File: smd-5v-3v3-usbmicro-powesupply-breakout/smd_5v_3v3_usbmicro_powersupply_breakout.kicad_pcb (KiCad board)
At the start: 2 copper layers, 40 x 40 mm, 11 parts, among them J1 USB_B_Micro, J2 SMD Pads, J3 THT Pins, U1 LMS1585AIS-3.3

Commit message: Better placement of components on pcb
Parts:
- moved C5 9.43 mm to (171.0, 124.0), turned to -90 degrees
- moved C4 8.94 mm to (153.0, 117.0), turned to 180 degrees
- moved C3 5.94 mm to (148.2, 109.0), turned to 180 degrees
- moved C2 4.40 mm to (155.0, 112.2), turned to 90 degrees
- moved FB1 4.00 mm to (157.0, 125.0)
- moved U1 1.46 mm to (167.0, 114.5)
- moved C1 1.00 mm to (160.0, 130.0)
- moved D1 1.00 mm to (160.0, 133.0)
- moved J3 1.00 mm to (158.0, 107.0)

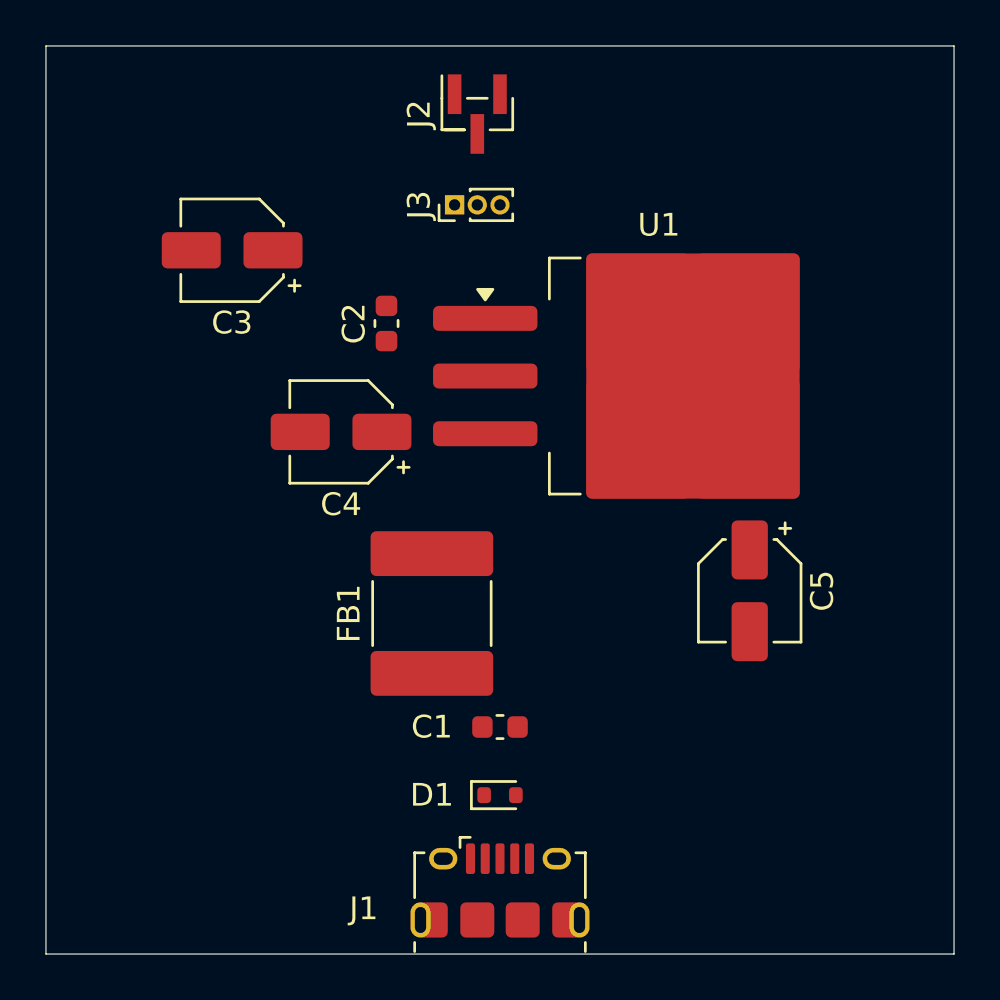
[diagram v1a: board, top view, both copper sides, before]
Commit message: Narrow pcb edge cuts
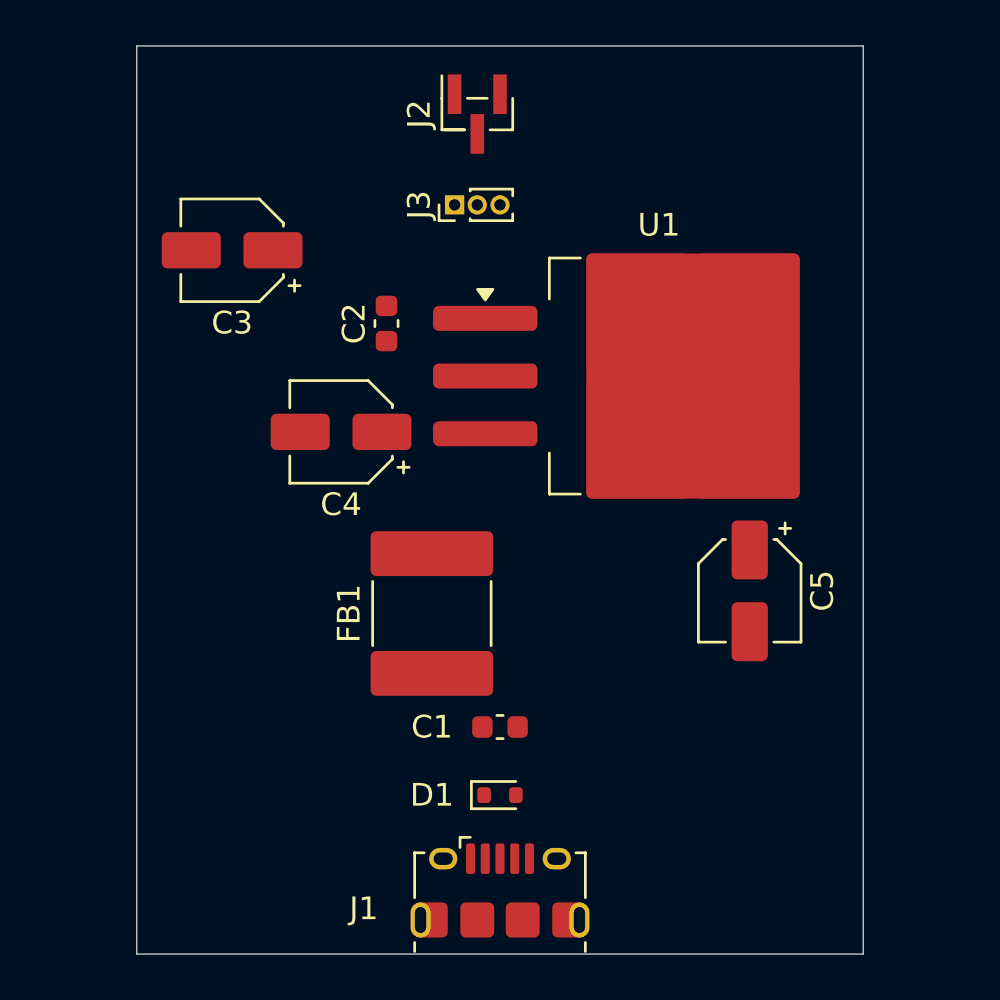
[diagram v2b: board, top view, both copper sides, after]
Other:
- board size 40 x 40 mm -> 32 x 40 mm
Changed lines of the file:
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@@
 		(tags "capacitor electrolytic")
 		(property "Reference" "C3"
-			(at 0 -3.2 360)
+			(at 0 -3.2 0)
 			(layer "F.SilkS")
 			(effects
@@
 		)
 		(property "Value" "10u"
-			(at 0 3.2 360)
+			(at 0 3.2 0)
 			(layer "F.Fab")
 			(effects
@@
 		)
 		(fp_text user "${REFERENCE}"
-			(at 0 0 360)
+			(at 0 0 0)
 			(layer "F.Fab")
 			(effects
@@
 		(tags "capacitor electrolytic")
 		(property "Reference" "C4"
-			(at 0 -3.2 360)
+			(at 0 -3.2 0)
 			(layer "F.SilkS")
 			(effects
@@
 		)
 		(property "Value" "10u"
-			(at 0 3.2 360)
+			(at 0 3.2 0)
 			(layer "F.Fab")
 			(effects
@@
 		)
 		(fp_text user "${REFERENCE}"
-			(at 0 0 360)
+			(at 0 0 0)
 			(layer "F.Fab")
 			(effects
@@
 	)
 	(gr_rect
-		(start 140 100)
-		(end 180 140)
+		(start 144 100)
+		(end 176 140)
 		(stroke
 			(width 0.05)

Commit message: Add ground pours
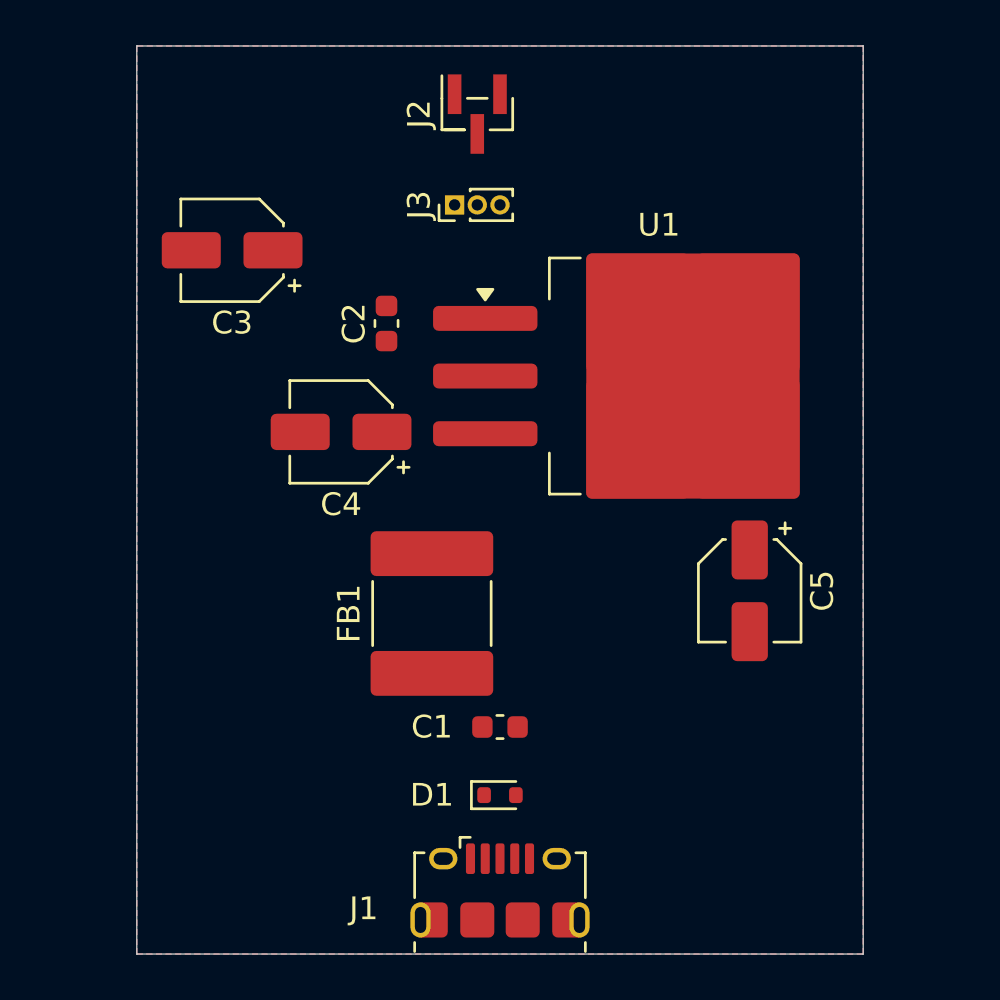
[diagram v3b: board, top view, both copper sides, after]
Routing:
- added copper zone on B.Cu, net GND
- added copper zone on F.Cu, net GND
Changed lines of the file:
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@@
 		(layer "Edge.Cuts")
 	)
+	(zone
+		(net 2)
+		(net_name "GND")
+		(layer "F.Cu")
+		(hatch edge 0.5)
+		(connect_pads
+			(clearance 0.5)
+		)
+		(min_thickness 0.25)
+		(filled_areas_thickness no)
+		(fill yes
+			(thermal_gap 0.5)
+			(thermal_bridge_width 0.5)
+		)
+		(polygon
+			(pts
+				(xy 144 100) (xy 144 140) (xy 176 140) (xy 176 100)
+			)
+		)
+	)
+	(zone
+		(net 2)
+		(net_name "GND")
+		(layer "B.Cu")
+		(hatch edge 0.5)
+		(priority 1)
+		(connect_pads
+			(clearance 0.5)
+		)
+		(min_thickness 0.25)
+		(filled_areas_thickness no)
+		(fill yes
+			(thermal_gap 0.5)
+			(thermal_bridge_width 0.5)
+		)
+		(polygon
+			(pts
+				(xy 144 100) (xy 144 140) (xy 176 140) (xy 176 100)
+			)
+		)
+	)
 )
